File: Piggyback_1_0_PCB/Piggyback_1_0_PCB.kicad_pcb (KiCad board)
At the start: 2 copper layers, 52.4 x 19.2 mm, 39 parts, among them J10 Conn_02x04_Odd_Even, J11 Conn_02x04_Odd_Even, J12 Conn_01x04_Female, J13 Conn_01x04_Female, J2 Conn_02x04_Odd_Even, J3 Conn_01x04_Female, J4 Conn_02x04_Odd_Even, J5 Conn_01x04_Female, J6 Conn_01x04_Female, J7 Conn_01x04_Female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

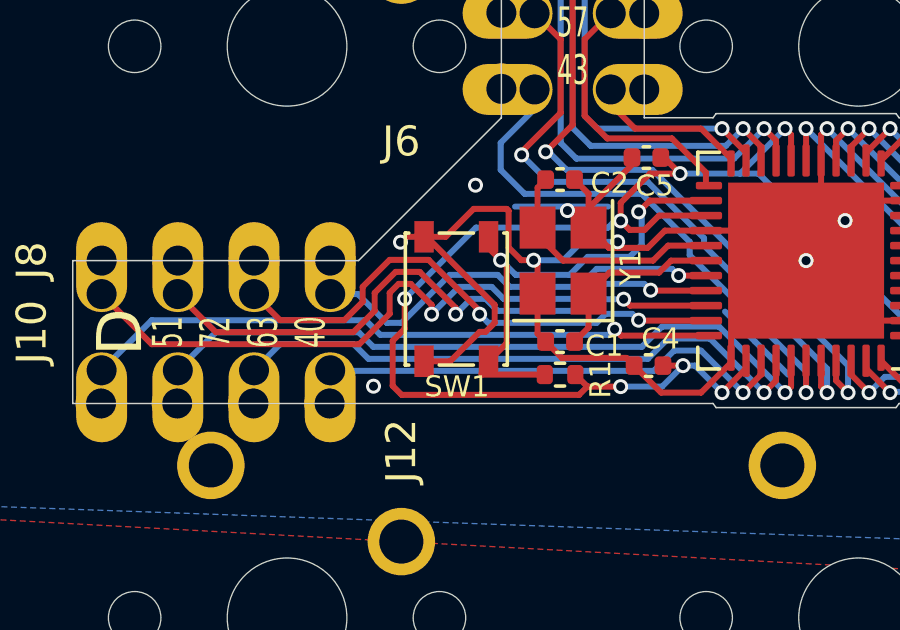
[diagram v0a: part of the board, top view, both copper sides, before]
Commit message: reset button clearance
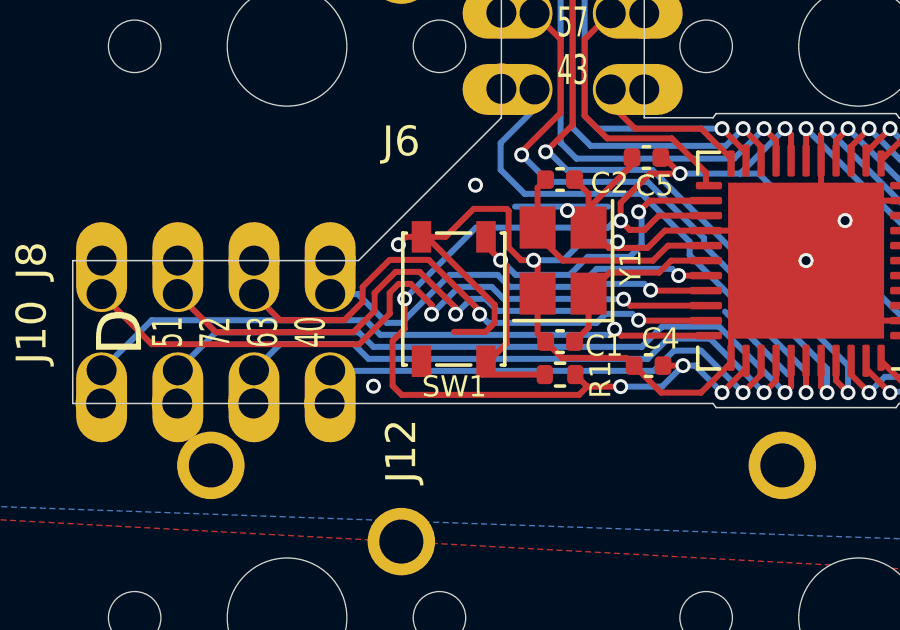
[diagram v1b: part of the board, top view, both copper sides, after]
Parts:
- moved SW1 0.09 mm to (72.2, 84.6)
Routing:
- net GND: track 105.6 -> 104.2 mm
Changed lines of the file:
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@@
   )
   (footprint "Button_Switch_SMD:SW_SPST_PTS810" (layer "F.Cu")
-    (at 72.317123 84.625014 90)
+    (at 72.23125 84.625 90)
     (descr "C&K Components, PTS 810 Series, Microminiature SMT Top Actuated, http://www.ckswitches.com/media/1476/pts810.pdf")
     (tags "SPST Button Switch")
@@
   (segment (start 93.593414 86.36375) (end 93.851082 86.106082) (width 0.2) (layer "F.Cu") (net 1))
   (segment (start 74.059743 81.683493) (end 74.059743 82.906575) (width 0.2) (layer "F.Cu") (net 1))
+  (segment (start 73.095 85.71875) (end 72.2375 85.71875) (width 0.2) (layer "F.Cu") (net 1))
   (segment (start 89.755 79.84375) (end 89.08 80.51875) (width 0.2) (layer "F.Cu") (net 1))
   (segment (start 93.59 86.36375) (end 93.593414 86.36375) (width 0.2) (layer "F.Cu") (net 1))
@@
   (segment (start 79.27 82.34375) (end 80.6375 82.34375) (width 0.2) (layer "F.Cu") (net 1))
   (segment (start 77.4 82.91875) (end 78.695 82.91875) (width 0.2) (layer "F.Cu") (net 1))
-  (segment (start 71.242123 86.700014) (end 72.113736 86.700014) (width 0.2) (layer "F.Cu") (net 1))
   (segment (start 76.725 81.59875) (end 78.245 80.07875) (width 0.2) (layer "F.Cu") (net 1))
   (segment (start 88.255 85.34375) (end 87.3125 85.34375) (width 0.2) (layer "F.Cu") (net 1))
@@
   (segment (start 92.12 80.04375) (end 92.545 79.61875) (width 0.2) (layer "F.Cu") (net 1))
   (segment (start 96.04375 86.63) (end 96.99375 86.63) (width 0.2) (layer "F.Cu") (net 1))
-  (segment (start 72.113736 86.700014) (end 73.095 85.71875) (width 0.2) (layer "F.Cu") (net 1))
   (segment (start 88.645 80.51875) (end 87.82 81.34375) (width 0.2) (layer "F.Cu") (net 1))
   (segment (start 84.475 79.14375) (end 84.675 78.94375) (width 0.2) (layer "F.Cu") (net 1))
@@
   (via (at 97.95625 82.13) (size 0.5) (drill 0.3) (layers "F.Cu" "B.Cu") (free) (net 1))
   (via (at 95.159732 83.452455) (size 0.5) (drill 0.3) (layers "F.Cu" "B.Cu") (net 1))
-  (via (at 70.45625 82.73) (size 0.5) (drill 0.3) (layers "F.Cu" "B.Cu") (free) (net 1))
+  (via (at 70.385707 82.811829) (size 0.5) (drill 0.3) (layers "F.Cu" "B.Cu") (free) (net 1))
   (via (at 92.545 79.61875) (size 0.5) (drill 0.3) (layers "F.Cu" "B.Cu") (net 1))
   (via (at 97.85625 86.43) (size 0.5) (drill 0.3) (layers "F.Cu" "B.Cu") (net 1))

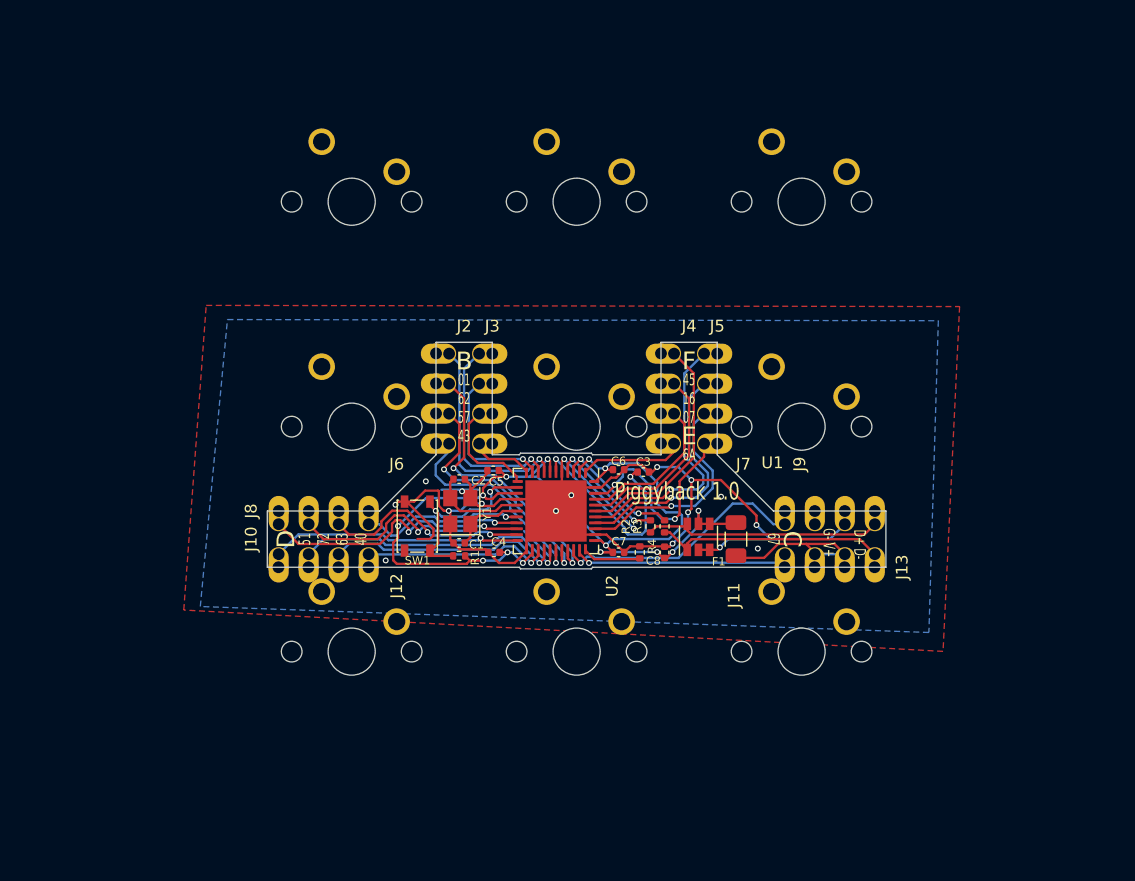
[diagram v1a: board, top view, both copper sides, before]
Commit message: smaller crystal
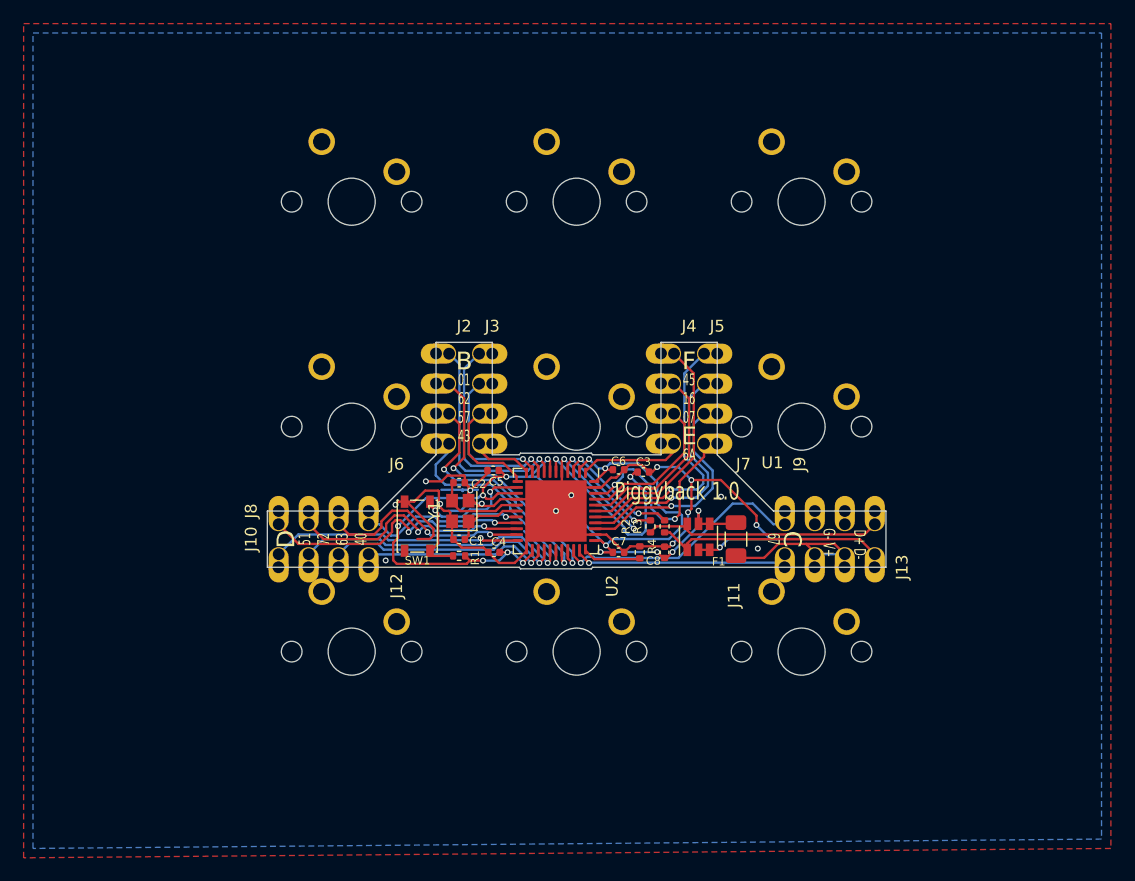
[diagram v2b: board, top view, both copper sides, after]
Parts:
- Y1: footprint Crystal:Crystal_SMD_3225-4Pin_3.2x2.5mm -> Crystal:Crystal_SMD_2520-4Pin_2.5x2.0mm
- moved C1 0.30 mm to (75.8, 85.7)
- moved C2 0.30 mm to (75.8, 80.9)
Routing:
- net GND: track 104.2 -> 107.4 mm

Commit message: Changes for FAB
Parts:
- removed MX1, MX2, MX3, MX4, MX5, MX6, MX7, MX8, MX9: MX-NoLED, MX_Only:MXOnly-1U-NoLED
- added REF**: breakaway-mousebites, Keebio-Parts:breakaway-mousebites, F.Cu at (111.9, 65.1)
- added REF**: breakaway-mousebites, Keebio-Parts:breakaway-mousebites, F.Cu at (76.2, 69.1)
- added REF**: breakaway-mousebites, Keebio-Parts:breakaway-mousebites, F.Cu at (95.2, 69.1)
- added REF**: breakaway-mousebites, Keebio-Parts:breakaway-mousebites, F.Cu at (111.9, 85.7)
- added REF**: breakaway-mousebites, Keebio-Parts:breakaway-mousebites, F.Cu at (59.5, 85.7)
- added REF**: breakaway-mousebites, Keebio-Parts:breakaway-mousebites, F.Cu at (59.5, 65.1)
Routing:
- net GND: vias 18 -> 17
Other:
- board size 52.4 x 19.2 mm -> 63.5 x 26.3 mm
- board text added: "Fiducial Here"
- board text added: "JLCJLCJLCJLC"

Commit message: created KiCad symbol and footprints for 1.0
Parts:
- added REF**: 1U, MX_Only:MXOnly-1U-NoLED, F.Cu at (104.8, 95.2)
- added REF**: 1U, MX_Only:MXOnly-1U-NoLED, F.Cu at (104.8, 76.2)
- added REF**: 1U, MX_Only:MXOnly-1U-NoLED, F.Cu at (85.7, 76.2)
- added REF**: 1U, MX_Only:MXOnly-1U-NoLED, F.Cu at (85.7, 95.2)
- added REF**: 1U, MX_Only:MXOnly-1U-NoLED, F.Cu at (66.7, 76.2)
- added REF**: 1U, MX_Only:MXOnly-1U-NoLED, F.Cu at (66.7, 95.2)
